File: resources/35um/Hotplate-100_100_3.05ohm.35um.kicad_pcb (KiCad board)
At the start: 2 copper layers, 100 x 100 mm, 7 parts, among them J1 Hotplate_Power_Connection, J2 Hotplate_Power_Connection

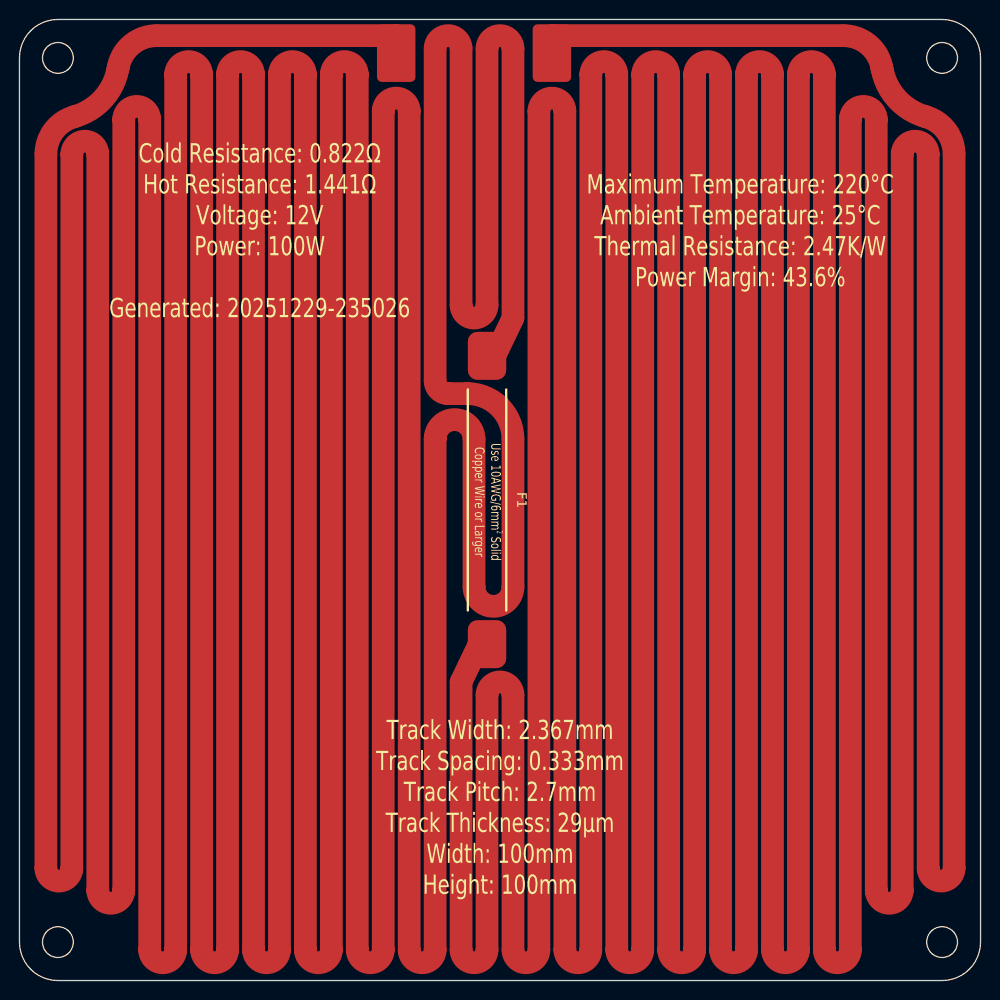
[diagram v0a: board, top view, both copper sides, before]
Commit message: Replaced obsolete 25mm thermal fuse footprint with new 35mm thermal fuse footprint.
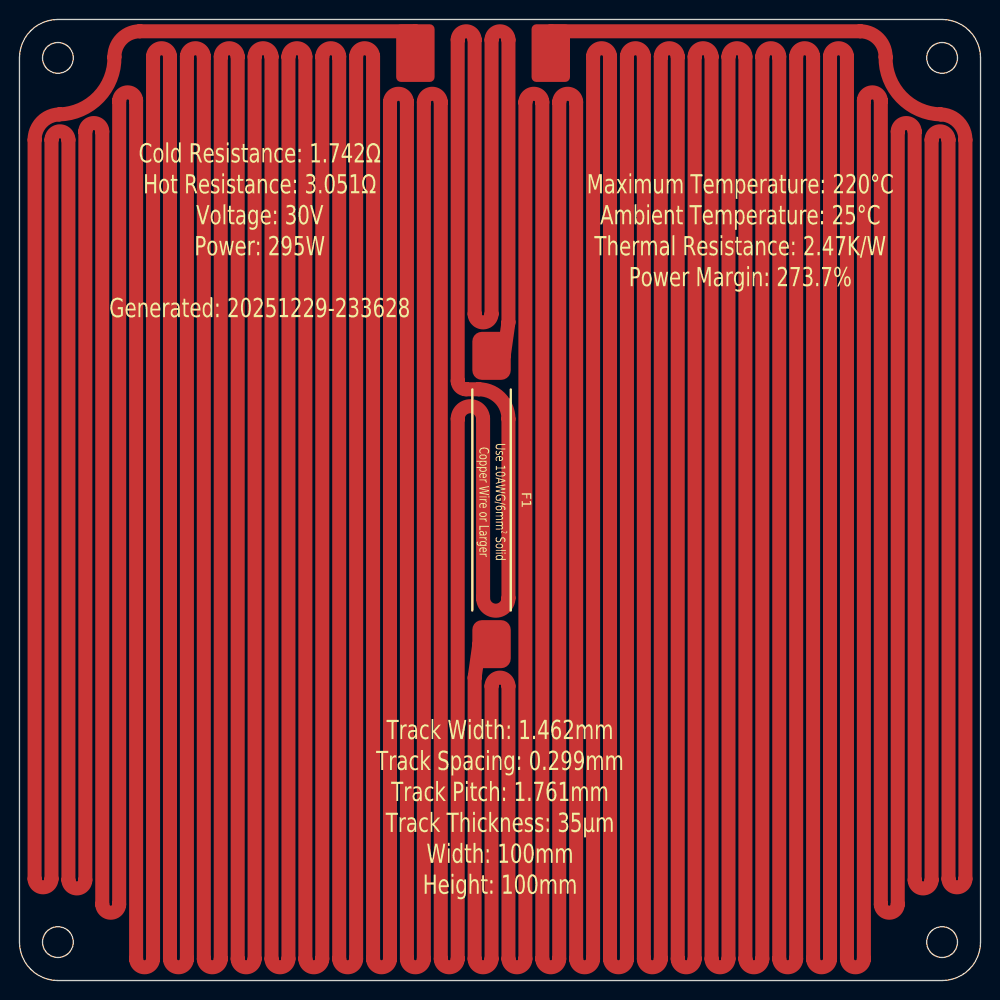
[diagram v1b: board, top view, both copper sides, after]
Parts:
- moved J1 2.00 mm to (96.2, 58.5)
- moved F1 0.47 mm to (104.1, 105.0)
- moved J2 0.12 mm to (110.3, 58.5)
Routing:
- net Net-(J1-Pin_1): track 1636.0 -> 2585.3 mm
- net Net-(J2-Pin_1): track 1685.6 -> 2634.8 mm
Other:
- board text added: "Cold Resistance: 1.742Ω Hot Resistance: 3.051Ω Voltage: 30V Power: 295W Generated: 20251229-233628"
- board text added: "Maximum Temperature: 220°C Ambient Temperature: 25°C Thermal Resistance: 2.47K/W Power Margin: 273.7%"
- board text added: "Track Width: 1.462mm Track Spacing: 0.299mm Track Pitch: 1.761mm Track Thickness: 35µm Width: 100mm Height: 100mm"
- board text removed: "Cold Resistance: 0.822Ω Hot Resistance: 1.441Ω Voltage: 12V Power: 100W Generated: 20251229-235026"
- board text removed: "Maximum Temperature: 220°C Ambient Temperature: 25°C Thermal Resistance: 2.47K/W Power Margin: 43.6%"
- board text removed: "Track Width: 2.367mm Track Spacing: 0.333mm Track Pitch: 2.7mm Track Thickness: 29µm Width: 100mm Height: 100mm"
